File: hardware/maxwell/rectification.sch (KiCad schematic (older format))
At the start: 25 parts, among them J19 Interconnect (Rect), K1 TXS2-L-3V, Q6 DMG2302UK, Q7 DMG2302UK, Q8 DMG2302UK, Q9 DMG2302UK, U15 LM74670-Q1, U16 LM74670-Q1, U17 LM74670-Q1, U18 LM74670-Q1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

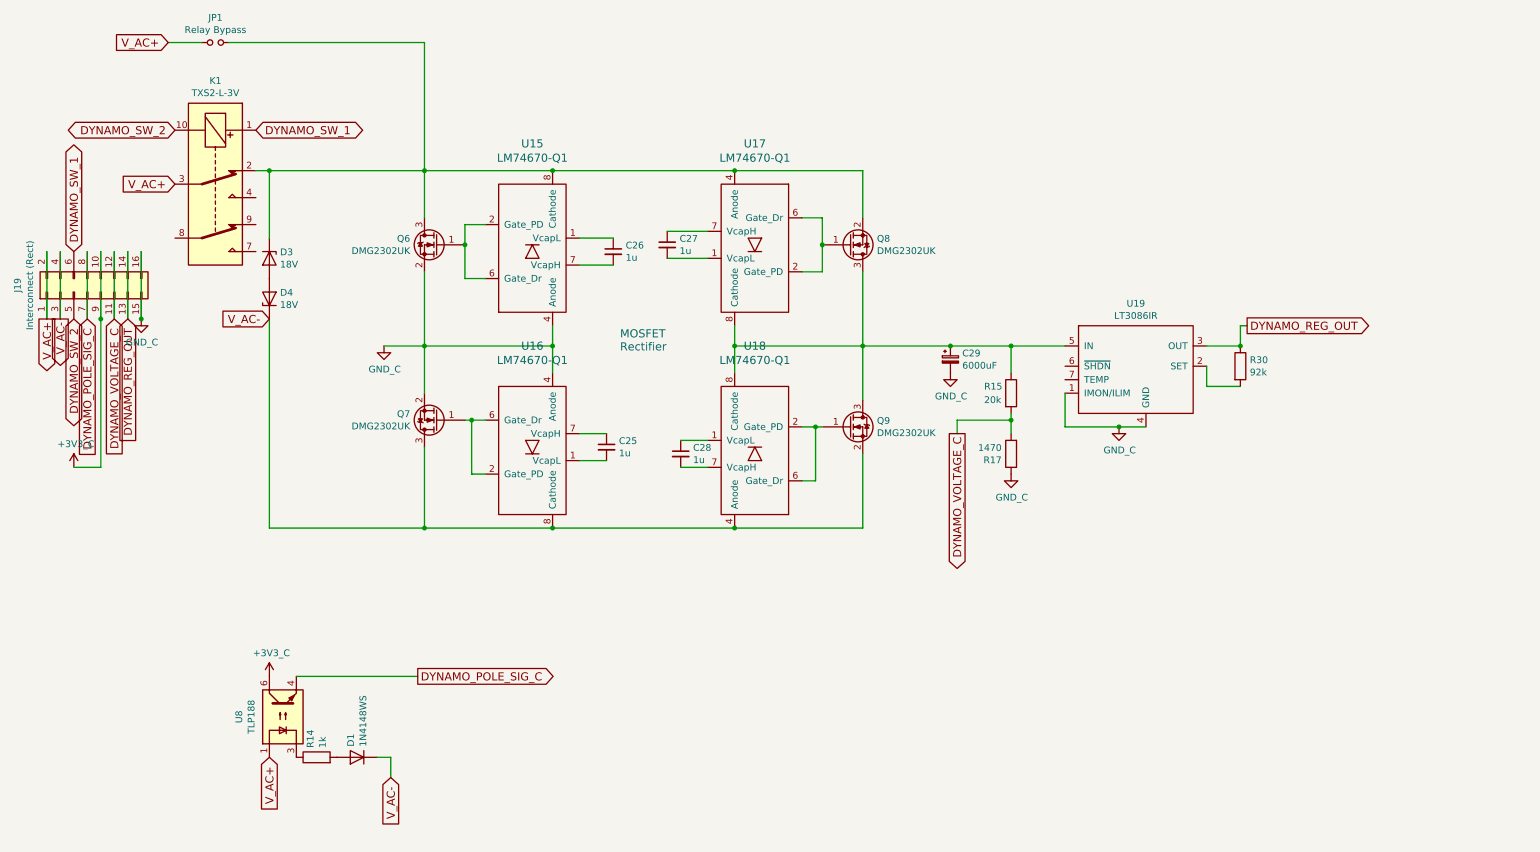
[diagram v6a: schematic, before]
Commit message: Adding Maxwell rect 1.9.10.
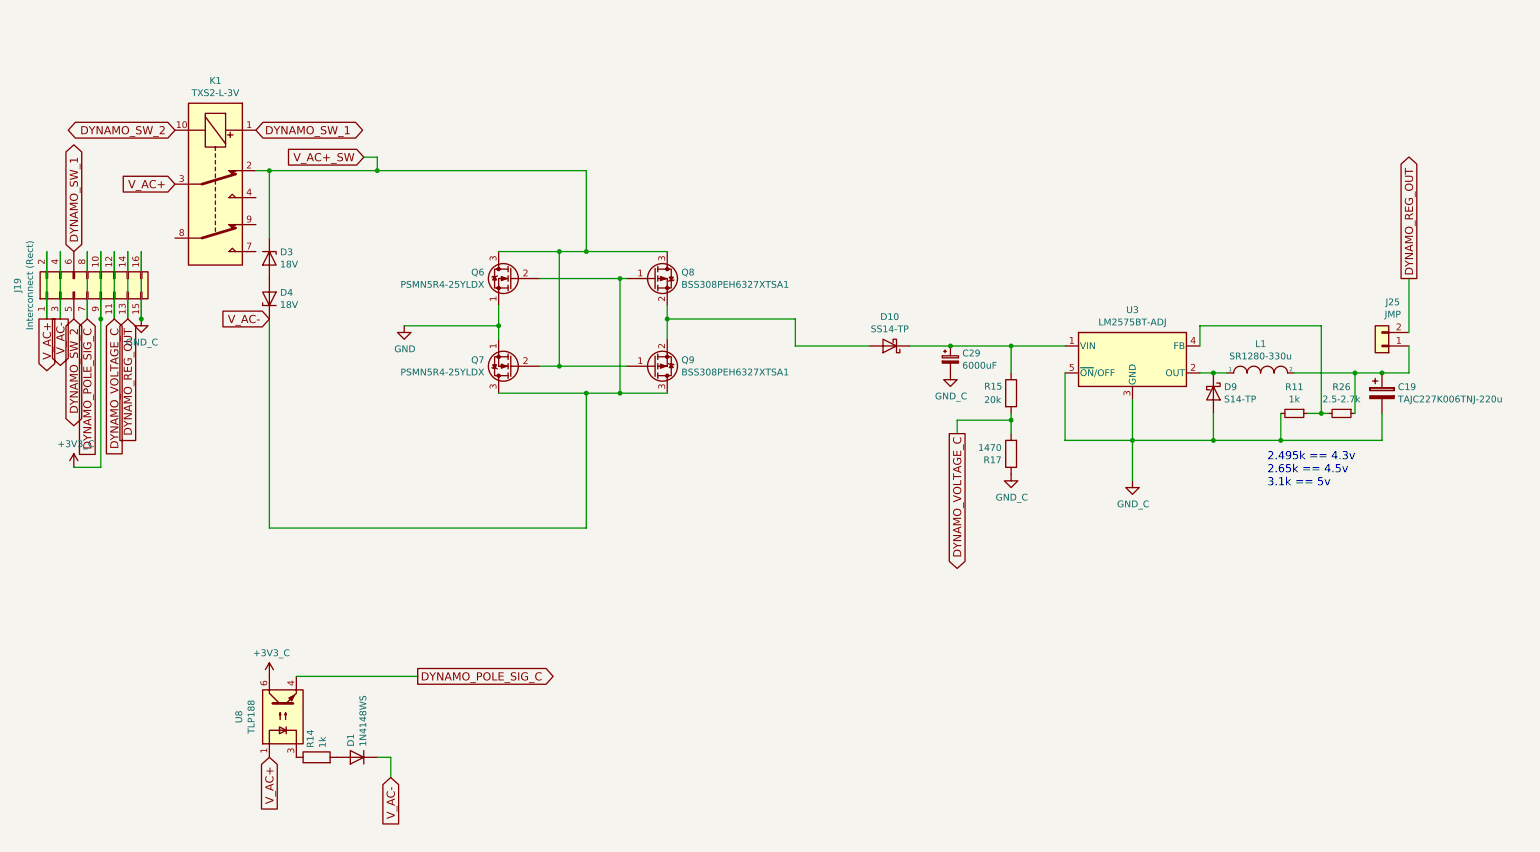
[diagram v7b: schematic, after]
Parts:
- removed C25, C26, C27, C28: 1u, coddingtonbear:0805_Milling, symbol Device:C_Small
- removed JP1: Relay Bypass, coddingtonbear:0805_Milling, symbol Device:Jumper_NO_Small
- removed Q6, Q7, Q8, Q9: DMG2302UK, coddingtonbear:SOT-23_LargePads, symbol Device:Q_NMOS_GSD
- removed R30: 92k, coddingtonbear:0805_Milling, symbol Device:R
- removed U15, U16, U17, U18: LM74670-Q1, Package_SO:VSSOP-8_3.0x3.0mm_P0.65mm, symbol coddingtonbear:LM74670-Q1
- removed U19: LT3086IR, Package_TO_SOT_SMD:TO-263-7_TabPin4, symbol coddingtonbear:LT3086IR
- added C19: TAJC227K006TNJ-220u, coddingtonbear:CP_Tantalum_Case-C_EIA-6032-28_Milling, symbol Device:CP
- added D10: SS14-TP, coddingtonbear:DO-214AC, symbol Device:D_Schottky
- added D9: S14-TP, coddingtonbear:DO-214AC, symbol Device:D_Schottky
- added J25: JMP, Connector_PinHeader_2.54mm:PinHeader_1x02_P2.54mm_Vertical, symbol Connector_Generic:Conn_01x02
- added L1: SR1280-330u, coddingtonbear:SRF1280-PARALLEL, symbol pspice:INDUCTOR
- added Q6, Q7: PSMN5R4-25YLDX, coddingtonbear:PSMN5R4-25YLD, symbol Device:Q_NMOS_SGD
- added Q8, Q9: BSS308PEH6327XTSA1, coddingtonbear:SOT-23_LargePads, symbol Device:Q_PMOS_GSD
- added R11: 1k, coddingtonbear:0805_Milling, symbol Device:R_Small
- added R26: 2.5-2.7k, coddingtonbear:0805_Milling, symbol Device:R_Small
- added U3: LM2575BT-ADJ, Package_TO_SOT_SMD:TO-263-5_TabPin3, symbol Regulator_Switching:LM2575BT-ADJ
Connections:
- net DYNAMO_REG_OUT: now also J25.2 (Pin_2)
- net GND_C: now also C19.2, D9.2 (A), R11.2, U3.3 (GND), U3.5 (~ON~/OFF)
- net V_AC-: now also Q6.2 (G), Q7.3 (D), Q8.1 (G), Q9.3 (D)
- net V_AC+_SW: now reaches D3.1 (K), K1.2
- net V_AC+_SW: now also Q6.3 (D), Q7.2 (G), Q8.3 (D), Q9.1 (G)
- net at C29.1, R15.1: now also D10.1 (K), U3.1 (VIN)
- new net: D9.1 (K), L1.1, U3.2 (OUT)
- new net: R11.1, R26.2, U3.4 (FB)
- new net: C19.1, J25.1 (Pin_1), L1.2, R26.1
- new net: D10.2 (A), Q8.2 (S), Q9.2 (S)
- new net GND: Q6.1 (S), Q7.1 (S)
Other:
- note added: "2.495k == 4.3v\n2.65k == 4.5v\n3.1k == 5v"
- note removed: "MOSFET\nRectifier"

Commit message: Maxwell-rect v 1.9.11; adds fixes for a couple minor oversights.
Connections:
- net GND is gone; now on net GND_C: Q6.1 (S), Q7.1 (S)
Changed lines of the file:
@@
 Wire Wire Line
 	4350 2650 4350 2800
-$Comp
-L power:GND #PWR0168
-U 1 1 5DB8C688
-P 3650 2800
-F 0 "#PWR0168" H 3650 2550 50  0001 C CNN
-F 1 "GND" H 3655 2627 50  0000 C CNN
-F 2 "" H 3650 2800 50  0001 C CNN
-F 3 "" H 3650 2800 50  0001 C CNN
-	1    3650 2800
-	1    0    0    -1
-$EndComp
 Wire Wire Line
 	3650 2800 4350 2800
@@
 Wire Wire Line
 	3450 1650 5000 1650
+$Comp
+L coddingtonbear:GND_C #PWR?
+U 1 1 5DB9EB94
+P 3650 2800
+F 0 "#PWR?" H 3650 2550 50  0001 C CNN
+F 1 "GND_C" H 3655 2627 50  0000 C CNN
+F 2 "" H 3650 2800 50  0001 C CNN
+F 3 "" H 3650 2800 50  0001 C CNN
+	1    3650 2800
+	1    0    0    -1
+$EndComp
 $EndSCHEMATC
